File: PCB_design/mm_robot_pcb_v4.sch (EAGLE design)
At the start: 35 parts, among them U1 PIC32

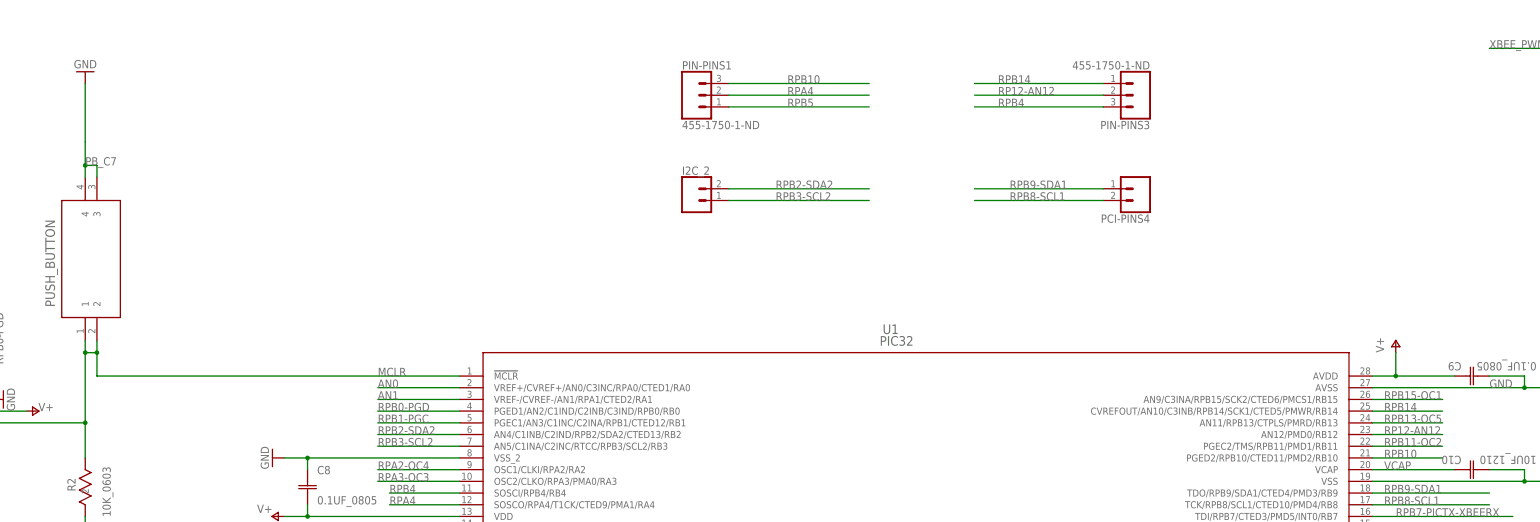
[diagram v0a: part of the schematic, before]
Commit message: Renamed PCB files so they're numbered correctly
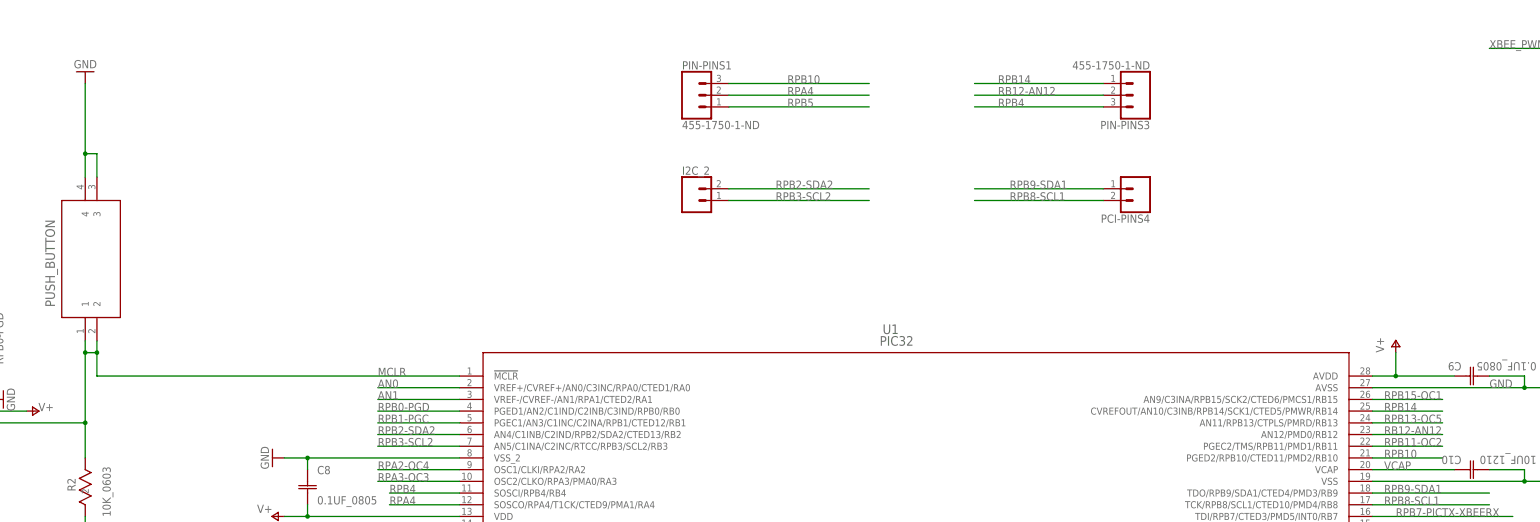
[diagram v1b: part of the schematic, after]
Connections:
- net RP12-AN12 renamed RB12-AN12
- removed net PB_C7: PIC_PB.3, PIC_PB.4
- net GND: now also PIC_PB.3, PIC_PB.4
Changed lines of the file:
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@@
 <junction x="134.62" y="-246.38"/>
+</segment>
+<segment>
+<pinref part="GND25" gate="1" pin="GND"/>
+<wire x1="-177.8" y1="-160.02" x2="-177.8" y2="-175.26" width="0.1524" layer="91"/>
+<wire x1="-177.8" y1="-175.26" x2="-175.26" y2="-175.26" width="0.1524" layer="91"/>
+<pinref part="PIC_PB" gate="A" pin="3"/>
+<wire x1="-175.26" y1="-175.26" x2="-175.26" y2="-180.34" width="0.1524" layer="91"/>
+<pinref part="PIC_PB" gate="A" pin="4"/>
+<wire x1="-177.8" y1="-175.26" x2="-177.8" y2="-180.34" width="0.1524" layer="91"/>
+<junction x="-177.8" y="-175.26"/>
 </segment>
 </net>
@@
 </segment>
 </net>
-<net name="PB_C7" class="0">
-<segment>
-<pinref part="PIC_PB" gate="A" pin="3"/>
-<wire x1="-175.26" y1="-180.34" x2="-175.26" y2="-177.8" width="0.1524" layer="91"/>
-<wire x1="-175.26" y1="-177.8" x2="-177.8" y2="-177.8" width="0.1524" layer="91"/>
-<pinref part="PIC_PB" gate="A" pin="4"/>
-<wire x1="-177.8" y1="-177.8" x2="-177.8" y2="-180.34" width="0.1524" layer="91"/>
-<wire x1="-177.8" y1="-177.8" x2="-177.8" y2="-172.72" width="0.1524" layer="91"/>
-<junction x="-177.8" y="-177.8"/>
-<label x="-177.8" y="-177.8" size="1.778" layer="95"/>
-<wire x1="-177.8" y1="-172.72" x2="-177.8" y2="-160.02" width="0.1524" layer="91"/>
-<pinref part="GND25" gate="1" pin="GND"/>
-</segment>
-</net>
 <net name="VCAP" class="0">
 <segment>
@@
 <wire x1="-38.1" y1="-160.02" x2="-7.62" y2="-160.02" width="0.1524" layer="91"/>
 <label x="-25.4" y="-160.02" size="1.778" layer="95"/>
-</segment>
-</net>
-<net name="RP12-AN12" class="0">
-<segment>
-<pinref part="U1" gate="A" pin="AN12/PMD0/RB12"/>
-<wire x1="101.6" y1="-236.22" x2="116.84" y2="-236.22" width="0.1524" layer="91"/>
-<label x="104.14" y="-236.22" size="1.778" layer="95"/>
-</segment>
-<segment>
-<pinref part="PIN-PINS3" gate="J$1" pin="2"/>
-<wire x1="43.18" y1="-162.56" x2="15.24" y2="-162.56" width="0.1524" layer="91"/>
-<label x="20.32" y="-162.56" size="1.778" layer="95"/>
 </segment>
 </net>
@@
 </segment>
 </net>
+<net name="RB12-AN12" class="0">
+<segment>
+<pinref part="U1" gate="A" pin="AN12/PMD0/RB12"/>
+<wire x1="101.6" y1="-236.22" x2="116.84" y2="-236.22" width="0.1524" layer="91"/>
+<label x="104.14" y="-236.22" size="1.778" layer="95"/>
+</segment>
+<segment>
+<pinref part="PIN-PINS3" gate="J$1" pin="2"/>
+<wire x1="43.18" y1="-162.56" x2="15.24" y2="-162.56" width="0.1524" layer="91"/>
+<label x="20.32" y="-162.56" size="1.778" layer="95"/>
+</segment>
+</net>
